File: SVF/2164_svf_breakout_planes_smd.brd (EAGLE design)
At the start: 63.5 x 99.7 mm, 88 parts, among them IC1 SSM2164S, IC2 TL072, IC3 TL072, IC4 TL072, IC5 TL072, IC6 TL072, U1 THONKICONNNEW, U2 THONKICONNNEW, U3 THONKICONNNEW, U4 THONKICONNNEW, U5 THONKICONNNEW, U6 THONKICONNNEW

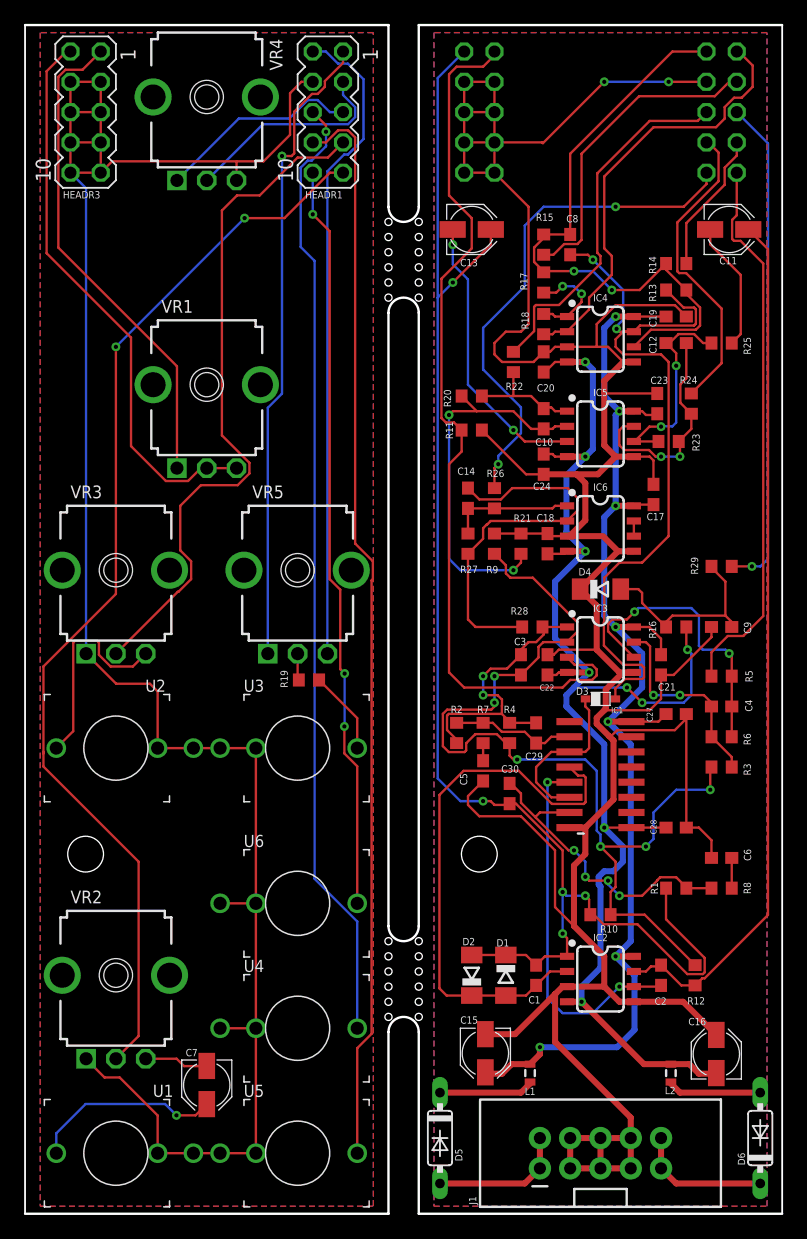
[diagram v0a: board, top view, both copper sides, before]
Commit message: Fix backwards footprint graphics for headers and power connector -- note that physical pinouts are unaffected
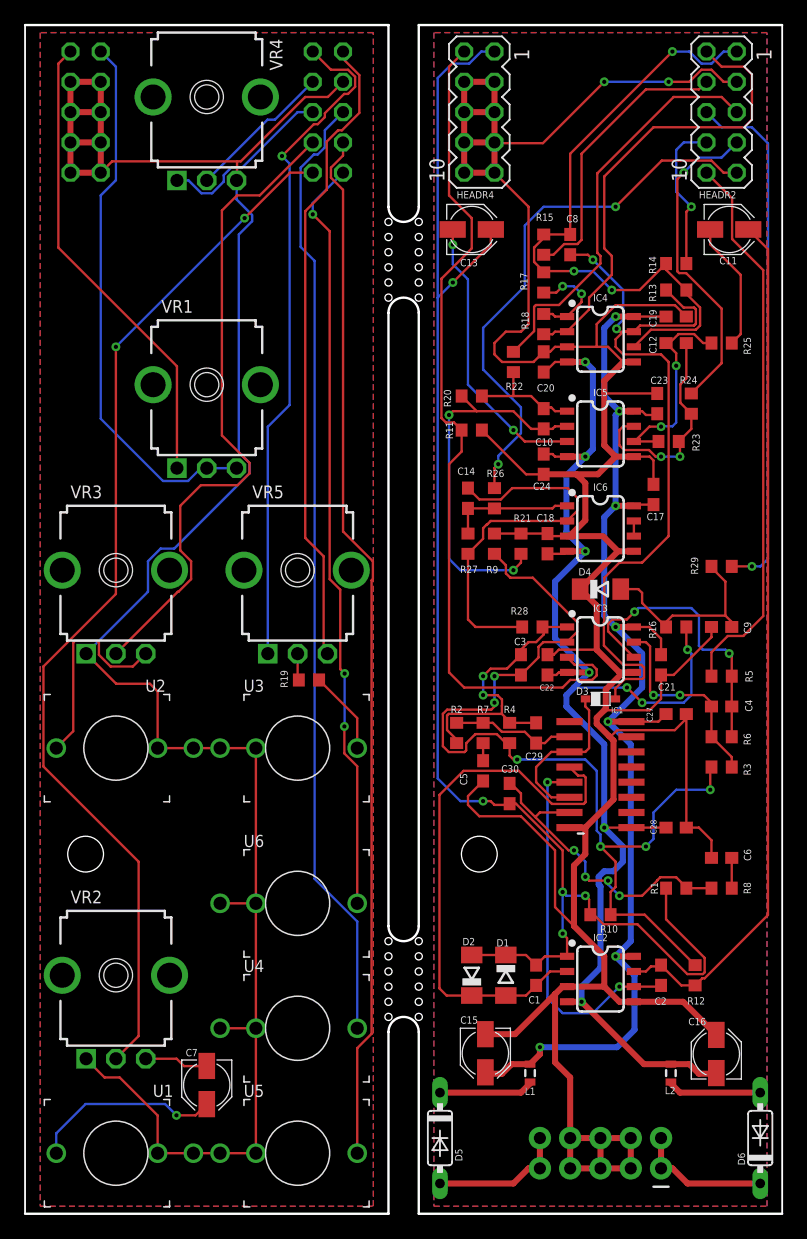
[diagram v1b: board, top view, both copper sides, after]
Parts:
- flipped HEADR1 to the top
- flipped HEADR2 to the bottom
- flipped HEADR3 to the top
- flipped HEADR4 to the bottom
- flipped J1 to the bottom
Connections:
- net N$42: now also J1.1, J1.2; no longer J1.10, J1.9
- net N$43: now also J1.10, J1.9; no longer J1.1, J1.2
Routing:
- net AGND: track 468.9 -> 477.2 mm
- net CUTOFF_POT1: track 18.0 -> 12.3 mm
- net TO_BP_CONN: track 30.5 -> 34.1 mm
- net LP_CONN: track 90.6 -> 87.2 mm
- net TO_CV2_POT1: track 52.4 -> 55.8 mm, vias 2 -> 3
- net TO_CV2_POT2: track 36.6 -> 39.7 mm
- net CV2_POT2: track 53.9 -> 56.8 mm
- net TO_HP_CONN: track 43.3 -> 46.2 mm
- net CV1_POT: track 57.9 -> 55.3 mm
- net TO_CUTOFF_POT2: track 41.9 -> 44.4 mm
- net TO_CUTOFF_POT1: track 26.4 -> 23.9 mm
- net TO_RESO_POT1: track 124.1 -> 126.7 mm
- net INPUT_POT: track 91.4 -> 88.9 mm
- net TO_RESO_POT2: track 75.1 -> 72.7 mm
- net CUTOFF_POT2: track 17.1 -> 15.0 mm
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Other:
- board text added: "kocmoc svf v 1.6 smd"
- board text removed: "kocmoc svf v 1.5 smd"

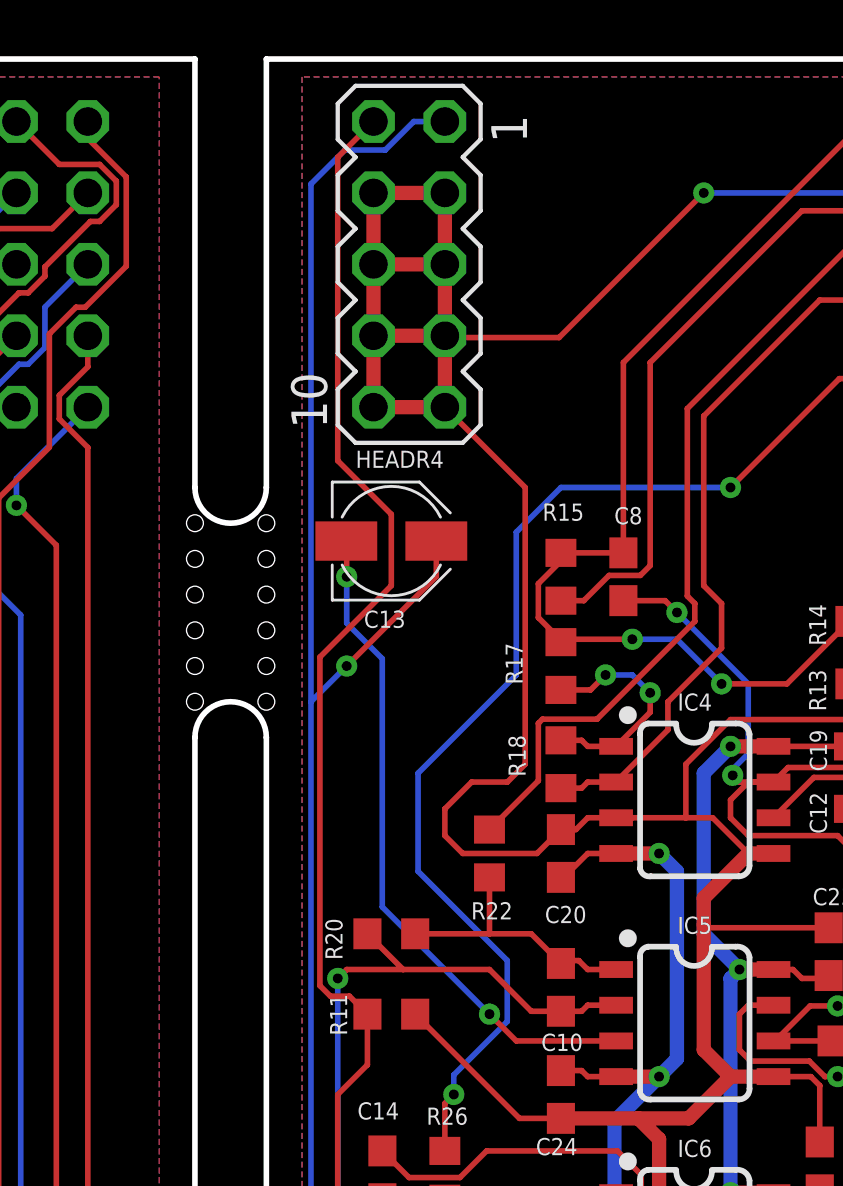
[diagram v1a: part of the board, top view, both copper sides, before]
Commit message: Fix bandpass output AC biasing issue
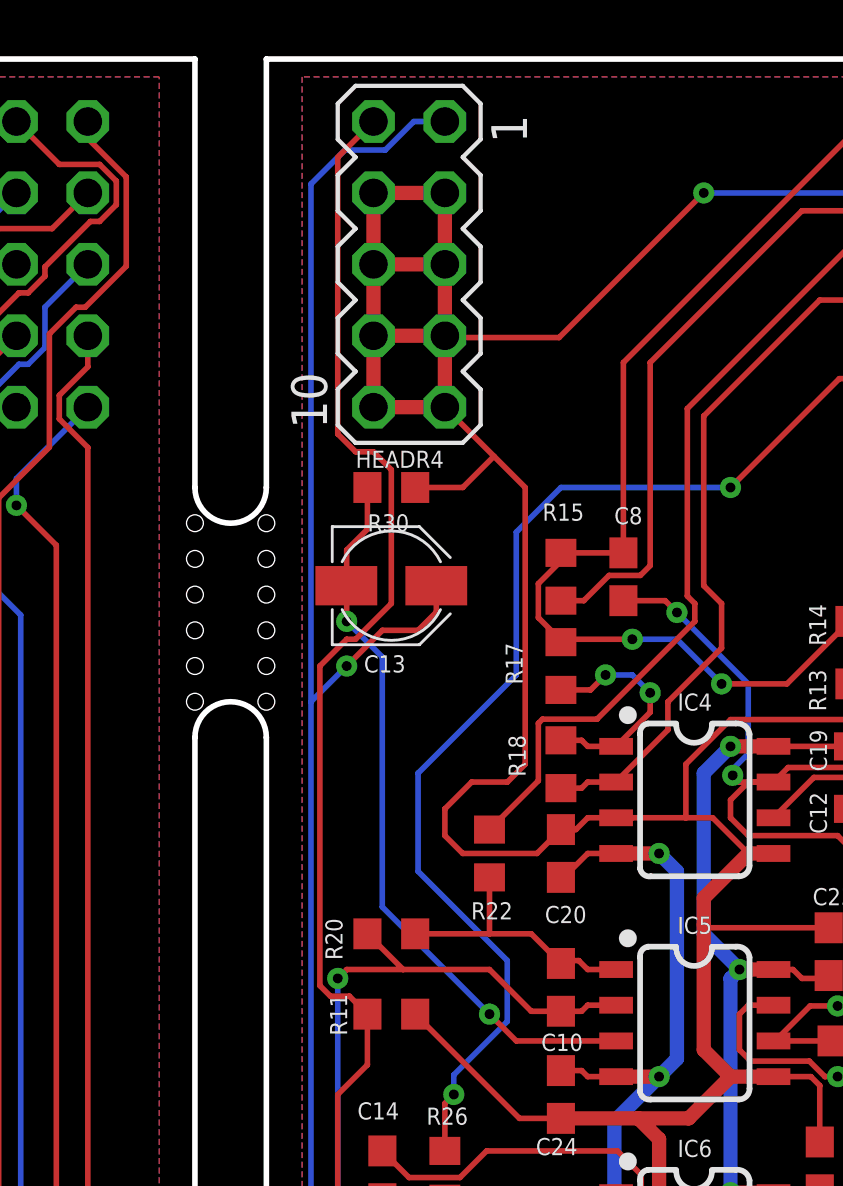
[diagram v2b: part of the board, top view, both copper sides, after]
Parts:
- added R30: 17k, rcl:R0603
- moved C13 1.59 mm to (37.5, 81.0)
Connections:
- net AGND: now also R30.1
- net N$30: now also R30.2
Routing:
- net AGND: track 477.2 -> 480.4 mm
- net N$30: track 23.8 -> 26.1 mm
- net TO_RESO_POT1: track 126.7 -> 125.8 mm
- net TO_RESO_POT2: track 72.7 -> 73.3 mm
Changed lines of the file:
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@@
 <attribute name="VALUE" x="51.181" y="70.866" size="0.6096" layer="27" ratio="10"/>
 </element>
-<element name="C13" library="rcl" library_urn="urn:adsk.eagle:library:334" package="PANASONIC_B" package3d_urn="urn:adsk.eagle:package:23421/2" value="2.2u" x="37.465" y="82.55" smashed="yes">
-<attribute name="NAME" x="37.973" y="80.0735" size="0.6096" layer="25" ratio="10" rot="R180"/>
-<attribute name="POPULARITY" value="4" x="84.455" y="5.08" size="1.778" layer="27" display="off"/>
-<attribute name="SPICEPREFIX" value="C" x="84.455" y="5.08" size="1.778" layer="27" display="off"/>
-<attribute name="VALUE" x="33.782" y="83.82" size="0.6096" layer="27" ratio="10"/>
+<element name="C13" library="rcl" library_urn="urn:adsk.eagle:library:334" package="PANASONIC_B" package3d_urn="urn:adsk.eagle:package:23421/2" value="2.2u" x="37.465" y="80.9625" smashed="yes">
+<attribute name="NAME" x="37.973" y="78.486" size="0.6096" layer="25" ratio="10" rot="R180"/>
+<attribute name="POPULARITY" value="4" x="84.455" y="3.4925" size="1.778" layer="27" display="off"/>
+<attribute name="SPICEPREFIX" value="C" x="84.455" y="3.4925" size="1.778" layer="27" display="off"/>
+<attribute name="VALUE" x="33.782" y="82.2325" size="0.6096" layer="27" ratio="10"/>
 </element>
 <element name="C14" library="rcl" library_urn="urn:adsk.eagle:library:334" package="C0603" package3d_urn="urn:adsk.eagle:package:23616/2" value="22p" x="37.1475" y="60.0075" smashed="yes" rot="R270">
@@
 </element>
 <element name="U$1" library="oshw" package="OSHW_5MM" value="" x="48.26" y="89.8525" smashed="yes" rot="SMR270"/>
+<element name="R30" library="rcl" library_urn="urn:adsk.eagle:library:334" package="R0603" package3d_urn="urn:adsk.eagle:package:23555/3" value="17k" x="37.465" y="84.455" smashed="yes" rot="R180">
+<attribute name="NAME" x="38.1" y="83.5025" size="0.6096" layer="25" rot="R180"/>
+<attribute name="POPULARITY" value="70" x="37.465" y="84.455" size="1.778" layer="27" rot="R180" display="off"/>
+<attribute name="SPICEPREFIX" value="R" x="37.465" y="84.455" size="1.778" layer="27" rot="R180" display="off"/>
+<attribute name="VALUE" x="38.1" y="86.36" size="1.27" layer="27" rot="R180"/>
+</element>
 </elements>
 <signals>
@@
 <wire x1="43.4326" y1="89.7876" x2="39.4349" y2="89.7876" width="0.2" layer="1"/>
 <wire x1="39.4349" y1="89.7876" x2="39.37" y2="89.8525" width="0.2" layer="1"/>
-<wire x1="42.2275" y1="84.455" x2="39.37" y2="87.3125" width="0.2" layer="1"/>
+<wire x1="42.2275" y1="84.455" x2="41.11625" y2="85.56625" width="0.2" layer="1"/>
+<wire x1="41.11625" y1="85.56625" x2="39.37" y2="87.3125" width="0.2" layer="1"/>
 <wire x1="56.72981875" y1="95.9469" x2="57.57018125" y2="95.9469" width="0.2" layer="1"/>
 <wire x1="53.975" y1="94.9325" x2="55.71541875" y2="94.9325" width="0.2" layer="1"/>
@@
 <wire x1="19.0456" y1="83.76370625" x2="17.74" y2="85.06930625" width="0.2" layer="16"/>
 <polygon width="0.2" layer="1">
-<vertex x="34.29" y="0.635"/>
-<vertex x="62.23" y="0.635"/>
-<vertex x="62.23" y="99.06"/>
-<vertex x="34.29" y="99.06"/>
-</polygon>
-<polygon width="0.2" layer="16">
-<vertex x="34.29" y="0.635"/>
-<vertex x="62.23" y="0.635"/>
-<vertex x="62.23" y="99.06"/>
-<vertex x="34.29" y="99.06"/>
-</polygon>
-<polygon width="0.2" layer="1">
 <vertex x="1.27" y="0.635"/>
 <vertex x="29.21" y="0.635"/>
@@
 <vertex x="1.27" y="99.06"/>
 </polygon>
-<wire x1="36.83" y1="94.9325" x2="26.67" y2="94.9325" width="0" layer="19" extent="1-1"/>
+<contactref element="R30" pad="1"/>
+<wire x1="38.315" y1="84.455" x2="40.005" y2="84.455" width="0.2" layer="1"/>
+<wire x1="40.005" y1="84.455" x2="41.11625" y2="85.56625" width="0.2" layer="1"/>
+<polygon width="0.2" layer="1">
+<vertex x="34.29" y="0.635"/>
+<vertex x="62.23" y="0.635"/>
+<vertex x="62.23" y="99.06"/>
+<vertex x="34.29" y="99.06"/>
+</polygon>
+<polygon width="0.2" layer="16">
+<vertex x="34.29" y="99.06"/>
+<vertex x="34.29" y="0.635"/>
+<vertex x="62.23" y="0.635"/>
+<vertex x="62.23" y="99.06"/>
+</polygon>
+<wire x1="26.67" y1="94.9325" x2="36.83" y2="94.9325" width="0" layer="19" extent="1-1"/>
 </signal>
 <signal name="N$2">
@@
 <wire x1="55.54295" y1="20.1001" x2="51.36295" y2="24.2801" width="0.2" layer="1"/>
 <wire x1="51.36295" y1="24.2801" x2="48.50545" y2="24.2801" width="0.2" layer="1"/>
-<wire x1="39.065" y1="82.55" x2="39.065" y2="81.2925" width="0.2" layer="1"/>
-<wire x1="39.065" y1="81.2925" x2="35.8775" y2="78.105" width="0.2" layer="1"/>
 <via x="35.8775" y="78.105" extent="1-16" drill="0.35"/>
 <wire x1="35.8775" y1="78.105" x2="34.6075" y2="76.835" width="0.2" layer="16"/>
@@
 <wire x1="35.8156" y1="96.4581" x2="37.25018125" y2="96.4581" width="0.2" layer="16"/>
 <wire x1="37.25018125" y1="96.4581" x2="38.26458125" y2="97.4725" width="0.2" layer="16"/>
+<wire x1="35.8775" y1="78.105" x2="37.1475" y2="79.375" width="0.2" layer="1"/>
+<wire x1="37.1475" y1="79.375" x2="38.4175" y2="79.375" width="0.2" layer="1"/>
+<wire x1="39.065" y1="80.0225" x2="39.065" y2="80.9625" width="0.2" layer="1"/>
+<wire x1="38.4175" y1="79.375" x2="39.065" y2="80.0225" width="0.2" layer="1"/>
 </signal>
 <signal name="N$4">
@@
 <contactref element="R11" pad="2"/>
 <contactref element="HEADR4" pad="2"/>
-<wire x1="37.465" y1="80.9625" x2="34.925" y2="78.4225" width="0.2" layer="1"/>
-<wire x1="37.465" y1="83.5025" x2="35.56" y2="85.4075" width="0.2" layer="1"/>
-<wire x1="37.465" y1="80.9625" x2="37.465" y2="83.5025" width="0.2" layer="1"/>
 <wire x1="35.9756" y1="66.3619" x2="36.615" y2="65.7225" width="0.2" layer="1"/>
 <wire x1="35.29879375" y1="66.3619" x2="35.9756" y2="66.3619" width="0.2" layer="1"/>
-<wire x1="34.925" y1="78.4225" x2="34.925" y2="66.73569375" width="0.2" layer="1"/>
+<wire x1="34.925" y1="66.73569375" x2="34.925" y2="78.105" width="0.2" layer="1"/>
 <wire x1="34.925" y1="66.73569375" x2="35.29879375" y2="66.3619" width="0.2" layer="1"/>
 <wire x1="36.615" y1="63.92" x2="36.615" y2="65.7225" width="0.2" layer="1"/>
@@
 <wire x1="35.56" y1="45.4025" x2="35.56" y2="62.865" width="0.2" layer="1"/>
 <wire x1="35.56" y1="96.2025" x2="36.83" y2="97.4725" width="0.2" layer="1"/>
-<wire x1="35.56" y1="85.4075" x2="35.56" y2="96.2025" width="0.2" layer="1"/>
+<wire x1="34.925" y1="78.105" x2="35.8775" y2="79.0575" width="0.2" layer="1"/>
+<wire x1="36.195" y1="79.0575" x2="37.465" y2="80.3275" width="0.2" layer="1"/>
+<wire x1="37.465" y1="80.3275" x2="37.465" y2="85.09" width="0.2" layer="1"/>
+<wire x1="37.465" y1="85.09" x2="36.83" y2="85.725" width="0.2" layer="1"/>
+<wire x1="35.8775" y1="79.0575" x2="36.195" y2="79.0575" width="0.2" layer="1"/>
+<wire x1="36.83" y1="85.725" x2="36.195" y2="85.725" width="0.2" layer="1"/>
+<wire x1="36.195" y1="85.725" x2="35.56" y2="86.36" width="0.2" layer="1"/>
+<wire x1="35.56" y1="86.36" x2="35.56" y2="96.2025" width="0.2" layer="1"/>
 </signal>
 <signal name="N$10">
@@
 <wire x1="40.9575" y1="65.7225" x2="41.91" y2="64.77" width="0.2" layer="1"/>
 <wire x1="41.91" y1="64.77" x2="45.46" y2="64.77" width="0.2" layer="1"/>
-<via x="35.8775" y="81.28" extent="1-16" drill="0.35"/>
-<wire x1="37.1431" y1="69.5369" x2="37.1431" y2="78.36620625" width="0.2" layer="16"/>
-<wire x1="35.8775" y1="79.63180625" x2="35.8775" y2="81.28" width="0.2" layer="16"/>
-<wire x1="37.1431" y1="78.36620625" x2="35.8775" y2="79.63180625" width="0.2" layer="16"/>
-<wire x1="35.8775" y1="81.28" x2="35.8775" y2="82.5375" width="0.2" layer="1"/>
-<wire x1="35.8775" y1="82.5375" x2="35.865" y2="82.55" width="0.2" layer="1"/>
-<wire x1="40.9575" y1="65.7225" x2="37.1431" y2="69.5369" width="0.2" layer="16"/>
+<wire x1="37.1431" y1="69.5369" x2="40.9575" y2="65.7225" width="0.2" layer="16"/>
+<contactref element="R30" pad="2"/>
+<wire x1="36.615" y1="84.455" x2="36.615" y2="82.97" width="0.2" layer="1"/>
+<wire x1="36.615" y1="82.97" x2="35.8775" y2="82.2325" width="0.2" layer="1"/>
+<wire x1="35.8775" y1="82.2325" x2="35.8775" y2="80.95" width="0.2" layer="1"/>
+<wire x1="35.865" y1="80.9625" x2="35.8775" y2="80.95" width="0.2" layer="1"/>
+<wire x1="35.8775" y1="80.95" x2="35.8775" y2="79.6925" width="0.2" layer="1"/>
+<via x="35.8775" y="79.6925" extent="1-16" drill="0.35"/>
+<wire x1="35.8775" y1="79.6925" x2="37.1431" y2="78.4269" width="0.2" layer="16"/>
+<wire x1="37.1431" y1="78.4269" x2="37.1431" y2="69.5369" width="0.2" layer="16"/>
 </signal>
 <signal name="N$31">
